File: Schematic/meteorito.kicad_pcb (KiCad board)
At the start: 2 copper layers, 80 x 66.1 mm, 8 parts, among them P1 DH22, P2 GY-ML8511, P3 BMP180, P4 CONN_01X08, P5 CONN_01X08

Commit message: Definicion de PCB
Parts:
- added P10: CONN_01X10, Connector_PinHeader_2.54mm:PinHeader_1x10_P2.54mm_Vertical, F.Cu at (118.1, 90.7)
- added P6: Hall, Connector_PinHeader_2.54mm:PinHeader_1x03_P2.54mm_Vertical, F.Cu at (123.2, 66.2)
- added P7: CONN_01X10, Connector_PinHeader_2.54mm:PinHeader_1x10_P2.54mm_Vertical, F.Cu at (83.0, 90.0)
- added P8: CONN_01X10, Connector_PinHeader_2.54mm:PinHeader_1x10_P2.54mm_Vertical, F.Cu at (94.3, 90.0)
- added P9: CONN_01X10, Connector_PinHeader_2.54mm:PinHeader_1x10_P2.54mm_Vertical, F.Cu at (106.8, 90.3)
- added R1: FOTORESISTENCIA, Resistor_THT:R_Axial_DIN0204_L3.6mm_D1.6mm_P2.54mm_Vertical, F.Cu at (113.0, 122.8)
- added R2: 100, Resistor_THT:R_Axial_DIN0204_L3.6mm_D1.6mm_P7.62mm_Horizontal, F.Cu at (132.4, 122.8)
- P4, P5: value CONN_01X08 -> Hall; footprint Pin_Headers:Pin_Header_Straight_1x08_Pitch2.54mm -> Connector_PinHeader_2.54mm:PinHeader_1x03_P2.54mm_Vertical
- moved G*** 90.4 mm to (74.7, 68.8)
- moved G*** 71.6 mm to (55.8, 99.6)
- moved REF*** 68.6 mm to (74.3, 130.0)
- moved P5 65.6 mm to (95.6, 66.2)
- moved P1 48.5 mm to (140.4, 102.8)
- moved P4 46.1 mm to (109.7, 66.2)
- moved P3 21.5 mm to (167.5, 120.2)
- moved P2 20.7 mm to (167.9, 85.0)
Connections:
- P1 pad 1: Net-(P1-Pad1) -> /IO23
- P1 pad 2: Net-(P1-Pad2) -> +5V
- P1 pad 3: Net-(P1-Pad3) -> GND
- P2 pad 1: Net-(P2-Pad1) -> +5V
- P2 pad 3: Net-(P2-Pad3) -> GND
- P2 pad 4: Net-(P2-Pad4) -> /IO27
- P2 pad 5: Net-(P2-Pad5) -> +5V
- P3 pad 1: Net-(P3-Pad1) -> +5V
- P3 pad 2: Net-(P3-Pad2) -> GND
- P3 pad 3: Net-(P3-Pad3) -> /IO22
- P3 pad 4: Net-(P3-Pad4) -> /IO21
- P4 pad 1: Net-(P4-Pad1) -> GND
- P4 pad 2: Net-(P4-Pad2) -> +5V
- P4 pad 3: Net-(P4-Pad3) -> /IO25
- P5 pad 1: Net-(P5-Pad1) -> GND
- P5 pad 2: Net-(P5-Pad2) -> +5V
- P5 pad 3: Net-(P5-Pad3) -> /IO17
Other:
- board size 80 x 66.1 mm -> 152.2 x 89.4 mm
- board text removed: "By"
- board text removed: "Humedad y Temperatura"
- board text removed: "Luz Ultravioleta"
- board text removed: "Presión"
- board text removed: "The Inventor's House"
- board text removed: "for"

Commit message: Medidas iniciales
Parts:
- G***: moved to F.Cu
- moved P6 55.4 mm to (67.9, 62.2), turned to 90 degrees
- moved P2 43.9 mm to (124.1, 81.7)
- moved P3 43.7 mm to (124.4, 113.1)
- moved P10 41.3 mm to (77.1, 86.3), turned to 90 degrees
- moved R2 39.7 mm to (92.8, 119.9)
- moved REF*** 38.3 mm to (112.6, 130.1)
- moved G*** 36.3 mm to (111.0, 68.8), turned to 90 degrees
- moved R1 35.0 mm to (78.1, 119.9)
- moved P9 29.8 mm to (77.1, 88.8), turned to 90 degrees
- moved P4 29.1 mm to (80.9, 62.2), turned to 90 degrees
- moved P8 27.7 mm to (77.1, 111.7), turned to 90 degrees
- moved P1 26.0 mm to (114.5, 100.6)
- moved P7 24.9 mm to (77.1, 114.2), turned to 90 degrees
- moved P5 4.20 mm to (95.8, 62.0), turned to 90 degrees
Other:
- board size 152.2 x 89.4 mm -> 95.3 x 89.4 mm

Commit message: Rooteo
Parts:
- moved G*** 46.3 mm to (64.8, 65.8)
- moved P5 21.9 mm to (81.2, 78.3)
- moved P3 17.4 mm to (126.0, 95.8)
- moved P6 15.5 mm to (81.2, 70.2)
- moved P2 14.8 mm to (116.3, 94.3)
- moved R2 10.6 mm to (84.9, 127.0)
- moved P1 9.27 mm to (106.0, 96.9)
- moved R1 7.60 mm to (75.4, 127.0)
- moved P4 0.36 mm to (81.2, 62.0)
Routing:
- net +5V: track 0.00 -> 100.2 mm
- net /IO25: track 0.00 -> 85.6 mm
- net /IO16: track 0.00 -> 72.4 mm
- net /IO17: track 0.00 -> 61.9 mm
- net /IO27: track 0.00 -> 55.4 mm
- net /IO22: track 0.00 -> 53.4 mm
- net /IO21: track 0.00 -> 48.6 mm
- net /IO23: track 0.00 -> 23.5 mm
- net /IO13: track 0.00 -> 6.94 mm
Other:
- net class Default: trace_width 0.25 -> 0.3
- board text added: "ESP32"
- board text added: "Sensor Hall Anemómetro"
- board text added: "Sensor Hall Pluviómetro"
- board text added: "Sensor Hall Veleta"
- board text added: "Sensor Nubosidad"
- board text added: "Sensor Presión Atmosférica"
- board text added: "Sensor Radiacion UV"
- board text added: "Sensor Tempertura y Humedad"

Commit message: add zones ground
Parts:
- moved REF*** 64.6 mm to (122.2, 66.2)
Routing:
- added copper zone on B.Cu, net GND
- added copper zone on F.Cu, net GND
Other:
- board text added: "Board"
- board text added: "by"
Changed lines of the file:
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@@
-(kicad_pcb (version 20171130) (host pcbnew "(5.0.0)")
+(kicad_pcb (version 20171130) (host pcbnew "(5.0.0-3-g5ebb6b6)")
   (general
     (thickness 1.6)
-    (drawings 28)
+    (drawings 30)
     (tracks 85)
     (zones 0)
@@
   )
   (module Symbols:OSHW-Logo_11.4x12mm_SilkScreen (layer F.Cu)
-    (at 112.6 130.1 90)
+    (at 122.25 66.25 90)
     (descr "Open Source Hardware Logo")
     (tags "Logo OSHW")
@@
     )
   )
+  (gr_text by (at 64.65 74.55 90) (layer F.SilkS)
+    (effects (font (size 3 3) (thickness 0.5)))
+  )
+  (gr_text Board (at 63.1 96.6 90) (layer F.SilkS)
+    (effects (font (size 3 3) (thickness 0.5)))
+  )
   (gr_text ESP32 (at 88.9 100.5 90) (layer F.SilkS)
     (effects (font (size 1.5 1.5) (thickness 0.3)))
@@
   (segment (start 105.1 72.5) (end 102.8 70.2) (width 0.3) (layer B.Cu) (net 10))
   (segment (start 77.94 127) (end 84.88 127) (width 0.3) (layer F.Cu) (net 41))
+  (zone (net 4) (net_name GND) (layer F.Cu) (hatch edge 0.508)
+    (connect_pads (clearance 0.508))
+    (min_thickness 0.254)
+    (fill yes (arc_segments 16) (thermal_gap 0.508) (thermal_bridge_width 0.508))
+    (polygon
+      (pts
+        (xy 40.55 56.1) (xy 39.8 144.95) (xy 135.3 145.1) (xy 134.7 55.6)
+      )
+    )
+  )
+  (zone (net 4) (net_name GND) (layer B.Cu) (hatch edge 0.508)
+    (connect_pads (clearance 0.508))
+    (min_thickness 0.254)
+    (fill yes (arc_segments 16) (thermal_gap 0.508) (thermal_bridge_width 0.508))
+    (polygon
+      (pts
+        (xy 40.75 56.05) (xy 40.1 145.05) (xy 135.15 144.9) (xy 134.55 55.7)
+      )
+    )
+  )
 )

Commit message: PCB Terminada
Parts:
- added G***: LOGO, TIH:electronic_cats_logo_8x6, B.Cu at (116.8, 130.8)
- added G***: LOGO, LOGO, B.Cu at (58.4, 99.1)
- added G***: LOGO, LOGO, B.Cu at (130.8, 115.6)
- added REF***: OSHW-Logo_11.4x12mm_SilkScreen, Symbols:OSHW-Logo_11.4x12mm_SilkScreen, B.Cu at (116.8, 69.8)
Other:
- board text added: "Compatible con:"
- board text added: "Con apoyo de:"

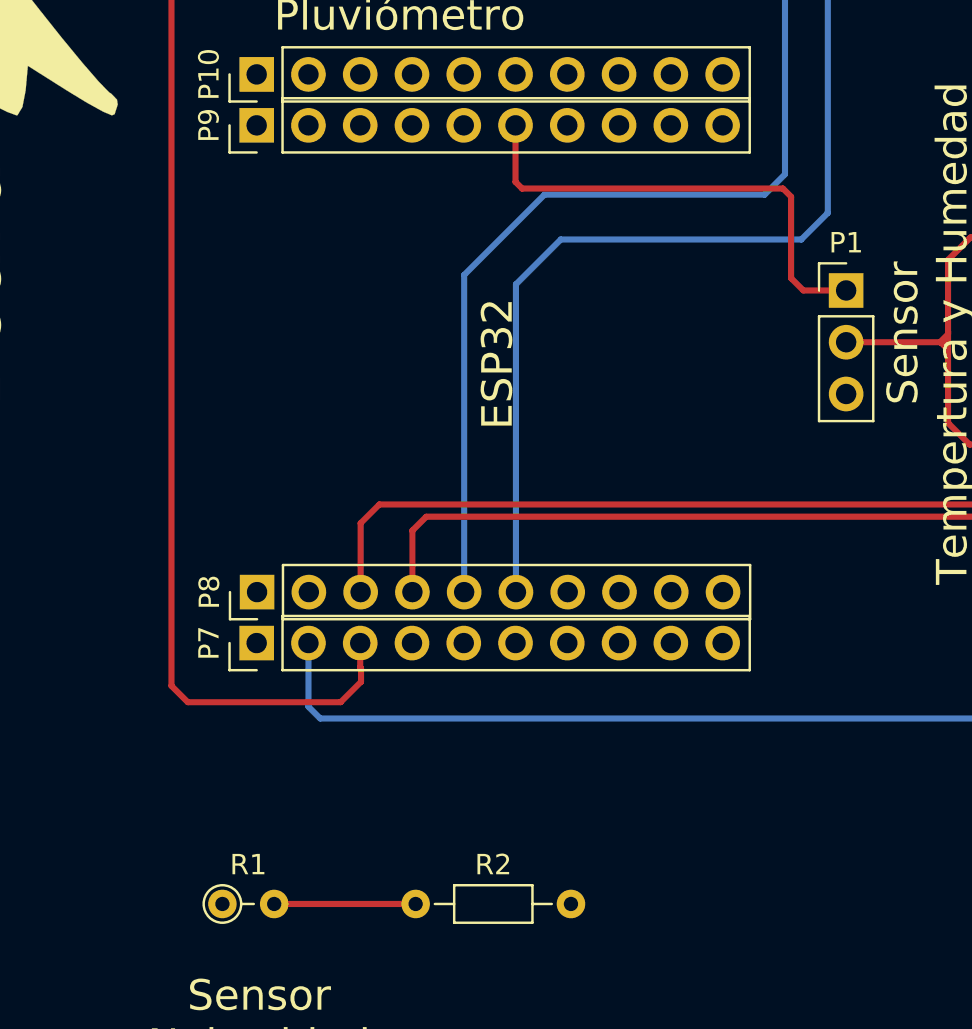
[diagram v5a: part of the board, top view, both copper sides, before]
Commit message: Corrección
Se colocaron la tierra y el VCC y se volvio a rootear lo faltante
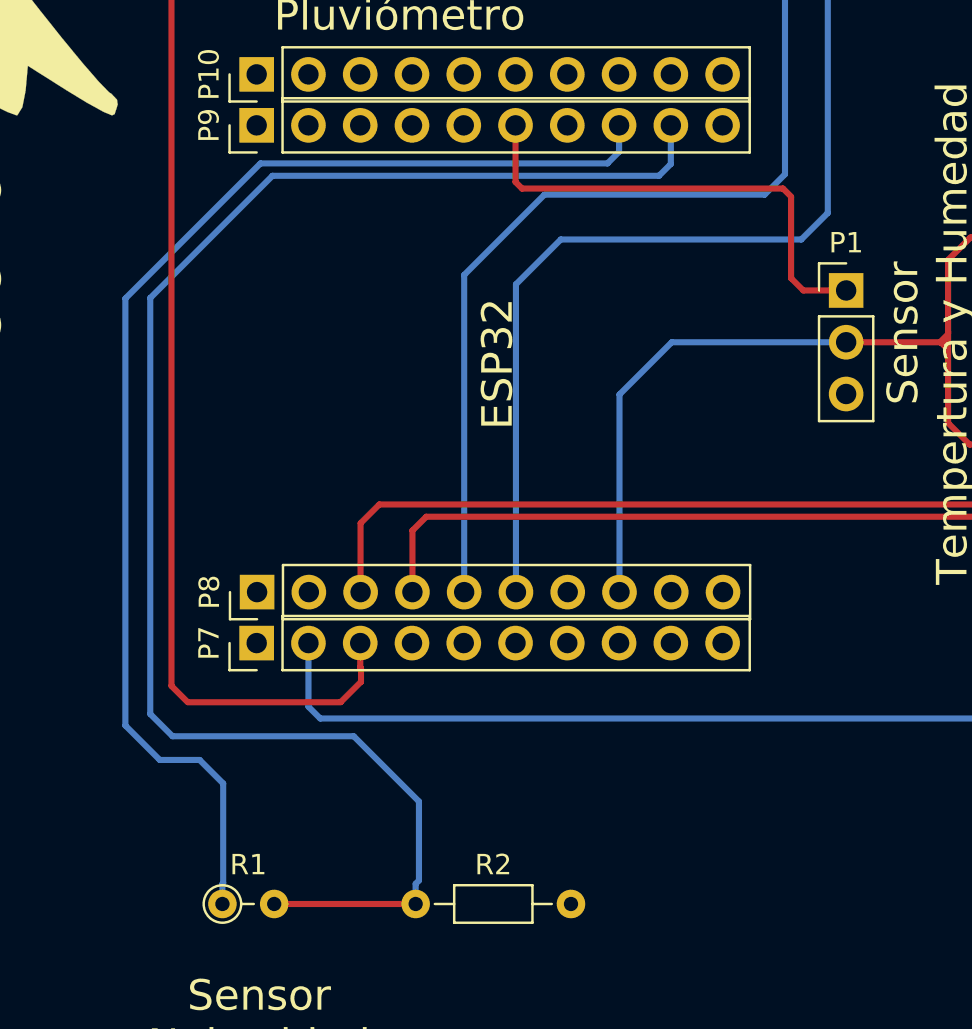
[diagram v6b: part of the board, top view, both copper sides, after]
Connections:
- P8 pad 8: /VCC -> +5V
- P9 pad 8: /3.3V -> +3V3
- P9 pad 9: /TCK -> /IO13
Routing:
- net /IO13: track 6.94 -> 77.6 mm
- net +3V3: track 0.00 -> 61.4 mm
- net +5V: track 100.2 -> 122.0 mm
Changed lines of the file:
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@@
     (thickness 1.6)
     (drawings 32)
-    (tracks 85)
+    (tracks 110)
     (zones 0)
     (modules 19)
-    (nets 42)
+    (nets 39)
   )
   (page A4)
@@
   (net 18 /TXD)
   (net 19 /RXD)
-  (net 20 /VCC)
-  (net 21 /TD0)
-  (net 22 /SD0)
-  (net 23 /RST)
-  (net 24 /SVP)
-  (net 25 "Net-(P9-Pad3)")
-  (net 26 "Net-(P9-Pad4)")
-  (net 27 "Net-(P9-Pad5)")
-  (net 28 /IO5)
-  (net 29 /3.3V)
-  (net 30 /TCK)
-  (net 31 /SD3)
-  (net 32 /CMD)
-  (net 33 /SD2)
-  (net 34 /NC)
-  (net 35 /TMS)
-  (net 36 /IO34)
-  (net 37 /IO33)
-  (net 38 /IO35)
-  (net 39 /SVN)
-  (net 40 +3V3)
-  (net 41 /IO13)
+  (net 20 /TD0)
+  (net 21 /SD0)
+  (net 22 /RST)
+  (net 23 /SVP)
+  (net 24 "Net-(P9-Pad3)")
+  (net 25 "Net-(P9-Pad4)")
+  (net 26 "Net-(P9-Pad5)")
+  (net 27 /IO5)
+  (net 28 /SD3)
+  (net 29 /CMD)
+  (net 30 /SD2)
+  (net 31 /NC)
+  (net 32 /TMS)
+  (net 33 /IO34)
+  (net 34 /IO33)
+  (net 35 /IO35)
+  (net 36 /SVN)
+  (net 37 +3V3)
+  (net 38 /IO13)
   (net_class Default "Esta es la clase de red por defecto."
     (clearance 0.2)
@@
     (add_net +3V3)
     (add_net +5V)
-    (add_net /3.3V)
     (add_net /CLK)
     (add_net /CMD)
@@
     (add_net /SVN)
     (add_net /SVP)
-    (add_net /TCK)
     (add_net /TD0)
     (add_net /TDI)
     (add_net /TMS)
     (add_net /TXD)
-    (add_net /VCC)
     (add_net GND)
     (add_net "Net-(P2-Pad2)")
@@
       (net 4 GND))
     (pad 8 thru_hole oval (at 0 17.78 90) (size 1.7 1.7) (drill 1) (layers *.Cu *.Mask)
-      (net 20 /VCC))
+      (net 3 +5V))
     (pad 9 thru_hole oval (at 0 20.32 90) (size 1.7 1.7) (drill 1) (layers *.Cu *.Mask)
-      (net 21 /TD0))
+      (net 20 /TD0))
     (pad 10 thru_hole oval (at 0 22.86 90) (size 1.7 1.7) (drill 1) (layers *.Cu *.Mask)
-      (net 22 /SD0))
+      (net 21 /SD0))
     (model ${KISYS3DMOD}/Connector_PinHeader_2.54mm.3dshapes/PinHeader_1x10_P2.54mm_Vertical.wrl
       (at (xyz 0 0 0))
@@
     )
     (pad 1 thru_hole rect (at 0 0 90) (size 1.7 1.7) (drill 1) (layers *.Cu *.Mask)
-      (net 23 /RST))
+      (net 22 /RST))
     (pad 2 thru_hole oval (at 0 2.54 90) (size 1.7 1.7) (drill 1) (layers *.Cu *.Mask)
-      (net 24 /SVP))
+      (net 23 /SVP))
     (pad 3 thru_hole oval (at 0 5.08 90) (size 1.7 1.7) (drill 1) (layers *.Cu *.Mask)
-      (net 25 "Net-(P9-Pad3)"))
+      (net 24 "Net-(P9-Pad3)"))
     (pad 4 thru_hole oval (at 0 7.62 90) (size 1.7 1.7) (drill 1) (layers *.Cu *.Mask)
-      (net 26 "Net-(P9-Pad4)"))
+      (net 25 "Net-(P9-Pad4)"))
     (pad 5 thru_hole oval (at 0 10.16 90) (size 1.7 1.7) (drill 1) (layers *.Cu *.Mask)
-      (net 27 "Net-(P9-Pad5)"))
+      (net 26 "Net-(P9-Pad5)"))
     (pad 6 thru_hole oval (at 0 12.7 90) (size 1.7 1.7) (drill 1) (layers *.Cu *.Mask)
       (net 2 /IO23))
     (pad 7 thru_hole oval (at 0 15.24 90) (size 1.7 1.7) (drill 1) (layers *.Cu *.Mask)
-      (net 28 /IO5))
+      (net 27 /IO5))
     (pad 8 thru_hole oval (at 0 17.78 90) (size 1.7 1.7) (drill 1) (layers *.Cu *.Mask)
-      (net 29 /3.3V))
+      (net 37 +3V3))
     (pad 9 thru_hole oval (at 0 20.32 90) (size 1.7 1.7) (drill 1) (layers *.Cu *.Mask)
-      (net 30 /TCK))
+      (net 38 /IO13))
     (pad 10 thru_hole oval (at 0 22.86 90) (size 1.7 1.7) (drill 1) (layers *.Cu *.Mask)
-      (net 31 /SD3))
+      (net 28 /SD3))
     (model ${KISYS3DMOD}/Connector_PinHeader_2.54mm.3dshapes/PinHeader_1x10_P2.54mm_Vertical.wrl
       (at (xyz 0 0 0))
@@
     (fp_line (start -0.635 -1.27) (end 1.27 -1.27) (layer F.Fab) (width 0.1))
     (pad 10 thru_hole oval (at 0 22.86 90) (size 1.7 1.7) (drill 1) (layers *.Cu *.Mask)
-      (net 32 /CMD))
+      (net 29 /CMD))
     (pad 9 thru_hole oval (at 0 20.32 90) (size 1.7 1.7) (drill 1) (layers *.Cu *.Mask)
-      (net 33 /SD2))
+      (net 30 /SD2))
     (pad 8 thru_hole oval (at 0 17.78 90) (size 1.7 1.7) (drill 1) (layers *.Cu *.Mask)
-      (net 34 /NC))
+      (net 31 /NC))
     (pad 7 thru_hole oval (at 0 15.24 90) (size 1.7 1.7) (drill 1) (layers *.Cu *.Mask)
-      (net 35 /TMS))
+      (net 32 /TMS))
     (pad 6 thru_hole oval (at 0 12.7 90) (size 1.7 1.7) (drill 1) (layers *.Cu *.Mask)
-      (net 36 /IO34))
+      (net 33 /IO34))
     (pad 5 thru_hole oval (at 0 10.16 90) (size 1.7 1.7) (drill 1) (layers *.Cu *.Mask)
-      (net 37 /IO33))
+      (net 34 /IO33))
     (pad 4 thru_hole oval (at 0 7.62 90) (size 1.7 1.7) (drill 1) (layers *.Cu *.Mask)
-      (net 38 /IO35))
+      (net 35 /IO35))
     (pad 3 thru_hole oval (at 0 5.08 90) (size 1.7 1.7) (drill 1) (layers *.Cu *.Mask)
-      (net 39 /SVN))
+      (net 36 /SVN))
     (pad 2 thru_hole oval (at 0 2.54 90) (size 1.7 1.7) (drill 1) (layers *.Cu *.Mask)
-      (net 34 /NC))
+      (net 31 /NC))
     (pad 1 thru_hole rect (at 0 0 90) (size 1.7 1.7) (drill 1) (layers *.Cu *.Mask)
       (net 4 GND))
@@
     )
     (pad 1 thru_hole circle (at 0 0) (size 1.4 1.4) (drill 0.7) (layers *.Cu *.Mask)
-      (net 40 +3V3))
+      (net 37 +3V3))
     (pad 2 thru_hole oval (at 2.54 0) (size 1.4 1.4) (drill 0.7) (layers *.Cu *.Mask)
-      (net 41 /IO13))
+      (net 38 /IO13))
     (model ${KISYS3DMOD}/Resistor_THT.3dshapes/R_Axial_DIN0204_L3.6mm_D1.6mm_P2.54mm_Vertical.wrl
       (at (xyz 0 0 0))
@@
     )
     (pad 1 thru_hole circle (at 0 0) (size 1.4 1.4) (drill 0.7) (layers *.Cu *.Mask)
-      (net 41 /IO13))
+      (net 38 /IO13))
     (pad 2 thru_hole oval (at 7.62 0) (size 1.4 1.4) (drill 0.7) (layers *.Cu *.Mask)
       (net 4 GND))
@@
   (segment (start 83.74 78.3) (end 83.74 70.2) (width 0.3) (layer F.Cu) (net 3))
   (segment (start 83.74 70.2) (end 83.74 62) (width 0.3) (layer F.Cu) (net 3))
+  (segment (start 106 99.44) (end 97.44556 99.44) (width 0.3) (layer B.Cu) (net 3))
+  (segment (start 94.88 102.00556) (end 94.88 111.7) (width 0.3) (layer B.Cu) (net 3))
+  (segment (start 97.44556 99.44) (end 94.88 102.00556) (width 0.3) (layer B.Cu) (net 3))
   (segment (start 115.097919 101.92) (end 115.077919 101.9) (width 0.3) (layer B.Cu) (net 5))
   (segment (start 116.3 101.92) (end 115.097919 101.92) (width 0.3) (layer B.Cu) (net 5))
@@
   (segment (start 102.8 70.2) (end 86.08 70.2) (width 0.3) (layer B.Cu) (net 10))
   (segment (start 105.1 72.5) (end 102.8 70.2) (width 0.3) (layer B.Cu) (net 10))
-  (segment (start 77.94 127) (end 84.88 127) (width 0.3) (layer F.Cu) (net 41))
+  (segment (start 75.4 126.010051) (end 75.438 125.972051) (width 0.3) (layer B.Cu) (net 37))
+  (segment (start 75.4 127) (end 75.4 126.010051) (width 0.3) (layer B.Cu) (net 37))
+  (segment (start 75.438 125.972051) (end 75.438 121.08942) (width 0.3) (layer B.Cu) (net 37))
+  (segment (start 75.438 121.08942) (end 74.2823 119.93372) (width 0.3) (layer B.Cu) (net 37))
+  (segment (start 74.2823 119.93372) (end 72.3265 119.93372) (width 0.3) (layer B.Cu) (net 37))
+  (segment (start 72.3265 119.93372) (end 70.6374 118.24462) (width 0.3) (layer B.Cu) (net 37))
+  (segment (start 70.6374 118.24462) (end 70.6374 97.29724) (width 0.3) (layer B.Cu) (net 37))
+  (segment (start 70.6374 97.29724) (end 77.2668 90.66784) (width 0.3) (layer B.Cu) (net 37))
+  (segment (start 77.2668 90.66784) (end 94.29242 90.66784) (width 0.3) (layer B.Cu) (net 37))
+  (segment (start 94.86 90.10026) (end 94.86 88.8) (width 0.3) (layer B.Cu) (net 37))
+  (segment (start 94.29242 90.66784) (end 94.86 90.10026) (width 0.3) (layer B.Cu) (net 37))
+  (segment (start 77.94 127) (end 84.88 127) (width 0.3) (layer F.Cu) (net 38))
+  (segment (start 84.88 126.010051) (end 85.04174 125.848311) (width 0.3) (layer B.Cu) (net 38))
+  (segment (start 84.88 127) (end 84.88 126.010051) (width 0.3) (layer B.Cu) (net 38))
+  (segment (start 85.04174 125.848311) (end 85.04174 121.9708) (width 0.3) (layer B.Cu) (net 38))
+  (segment (start 85.04174 121.9708) (end 81.84134 118.7704) (width 0.3) (layer B.Cu) (net 38))
+  (segment (start 81.84134 118.7704) (end 72.95134 118.7704) (width 0.3) (layer B.Cu) (net 38))
+  (segment (start 72.95134 118.7704) (end 71.85914 117.6782) (width 0.3) (layer B.Cu) (net 38))
+  (segment (start 71.85914 117.6782) (end 71.85914 97.2693) (width 0.3) (layer B.Cu) (net 38))
+  (segment (start 71.85914 97.2693) (end 77.85354 91.2749) (width 0.3) (layer B.Cu) (net 38))
+  (segment (start 77.85354 91.2749) (end 96.81972 91.2749) (width 0.3) (layer B.Cu) (net 38))
+  (segment (start 97.4 90.69462) (end 97.4 88.8) (width 0.3) (layer B.Cu) (net 38))
+  (segment (start 96.81972 91.2749) (end 97.4 90.69462) (width 0.3) (layer B.Cu) (net 38))
   (zone (net 4) (net_name GND) (layer F.Cu) (hatch edge 0.508)
     (connect_pads (clearance 0.508))

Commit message: Nuevo Rooteo
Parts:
- moved G*** 33.6 mm to (126.2, 82.3)
- moved P2 23.5 mm to (119.8, 117.5)
- moved P3 23.1 mm to (130.5, 118.4)
- moved P1 22.2 mm to (113.6, 76.0)
- moved REF*** 15.0 mm to (102.0, 68.1)
- moved G*** 4.58 mm to (116.1, 135.3)
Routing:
- net /IO23: track 23.5 -> 88.0 mm
- net /IO21: track 48.6 -> 91.5 mm
- net /IO22: track 53.4 -> 83.6 mm
- net +5V: track 122.0 -> 143.8 mm
- net /IO27: track 55.4 -> 45.9 mm
- net /IO17: track 61.9 -> 69.3 mm
- net /IO16: track 72.4 -> 78.7 mm
